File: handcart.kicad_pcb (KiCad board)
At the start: 2 copper layers, 166 x 85 mm, 51 parts, among them J1 PANEL, J10 FANS, J2 BMS, J3 Raspberry_Pi_2_3, J4 DB9_Female_DCE, J5 CHARGER, J8 POWER, K1 EX12U1S, Q1 2N7002NXAKR, Q2 NTR5105PT1G, Q3 NTR5105PT1G, Q4 2N7002NXAKR, Q5 NTR5105PT1G, Q6 2N7002NXAKR, Q7 2N7002NXAKR, SW1 SW_SPDT, U1 MCP2515-xSO, U2 MCP2562-E-SN, U3 MAX3232CDR, U4 Tex_DCDC, U5 L7805, Y1 16MHz

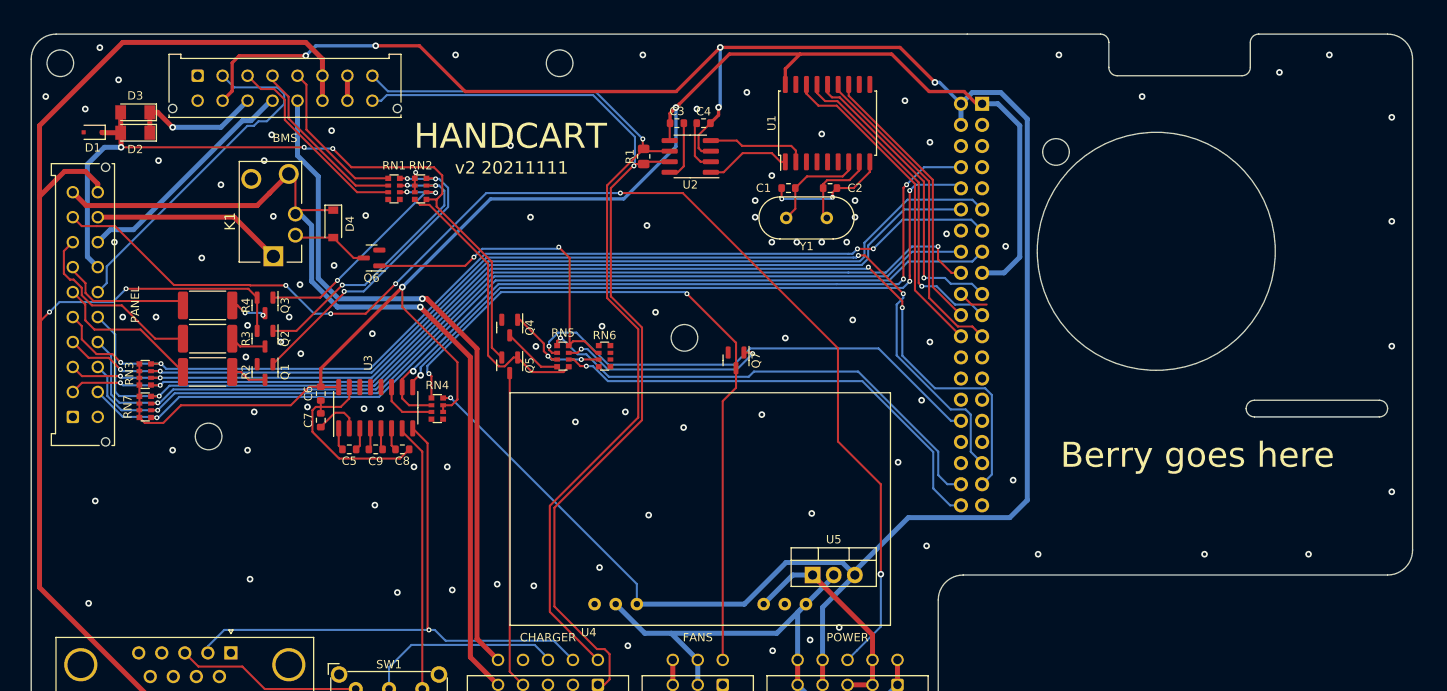
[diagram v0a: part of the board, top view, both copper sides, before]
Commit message: missing holes added
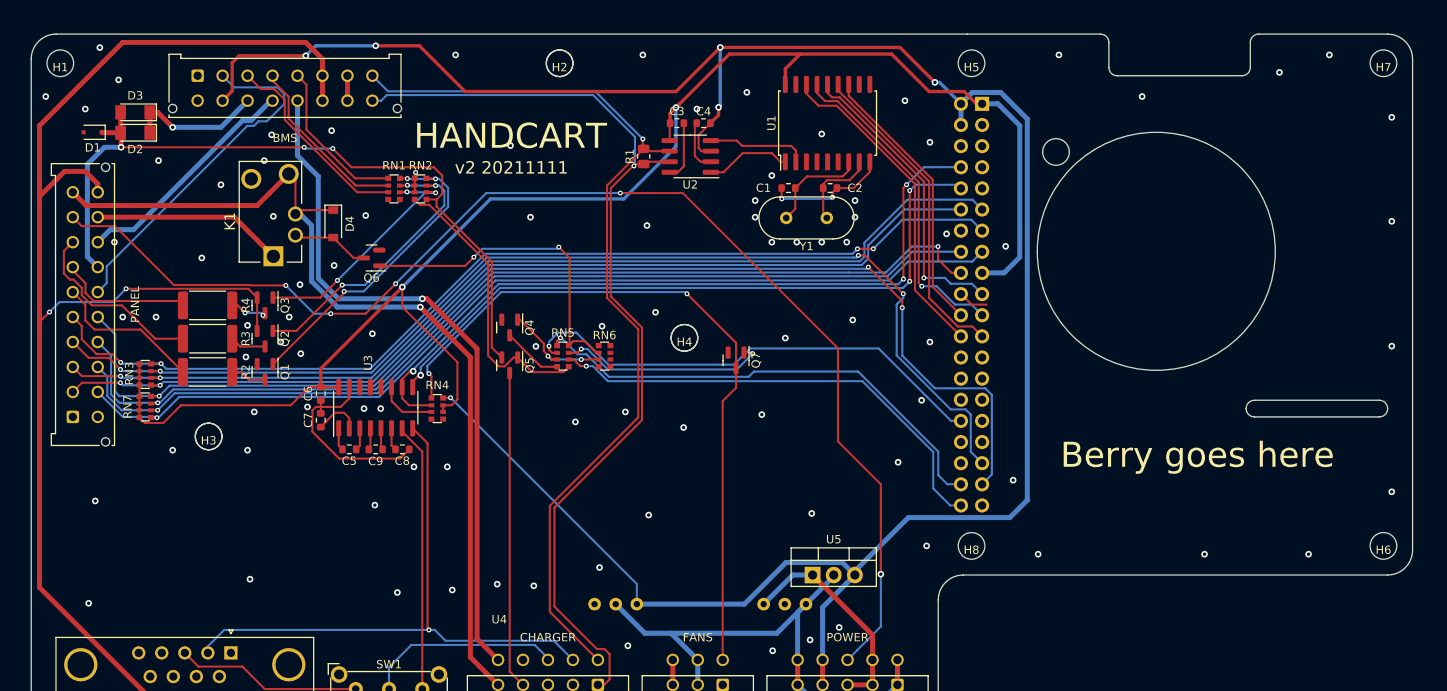
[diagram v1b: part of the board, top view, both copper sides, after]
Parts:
- removed the REF** at (105.2, 61.5)
- added H1: MountingHole, Eagle_Main:MountingHole_3.2_6.1Free, F.Cu at (105.2, 61.5)
- added H2: MountingHole, Eagle_Main:MountingHole_3.2_6.1Free, F.Cu at (165.2, 61.5)
- added H3: MountingHole, Eagle_Main:MountingHole_3.2_6.1Free, F.Cu at (123.0, 106.3)
- added H4: MountingHole, Eagle_Main:MountingHole_3.2_6.1Free, F.Cu at (180.2, 94.5)
- added H5: MountingHole, Eagle_Main:MountingHole_3.2_6.1Free, F.Cu at (214.7, 61.5)
- added H6: MountingHole, Eagle_Main:MountingHole_3.2_6.1Free, F.Cu at (264.2, 119.5)
- added H7: MountingHole, Eagle_Main:MountingHole_3.2_6.1Free, F.Cu at (264.2, 61.5)
- added H8: MountingHole, Eagle_Main:MountingHole_3.2_6.1Free, F.Cu at (214.7, 119.5)
- J3: footprint handcart:raspberrypi_hat_template -> Eagle_Main:raspberrypi_hat_template
- U4: footprint handcart:Tex_DCDC -> Eagle_Main:Tex_DCDC_horizontal
